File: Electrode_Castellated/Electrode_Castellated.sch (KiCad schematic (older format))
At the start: 21 parts, among them J1 Connector

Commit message: Switch to pogo pin style connector pads
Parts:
- J1: footprint Connector_PinHeader_2.54mm:PinHeader_2x10_P2.54mm_Vertical_SMD -> eaton:Millmax Pad Contacts
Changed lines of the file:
@@
 F 0 "J1" H 3768 4417 50  0000 C CNN
 F 1 "Connector" H 3768 4326 50  0000 C CNN
-F 2 "Connector_PinHeader_2.54mm:PinHeader_2x10_P2.54mm_Vertical_SMD" H 3850 3300 50  0001 C CNN
+F 2 "eaton:Millmax Pad Contacts" H 3850 3300 50  0001 C CNN
 F 3 "~" H 3850 3300 50  0001 C CNN
 	1    3850 3300

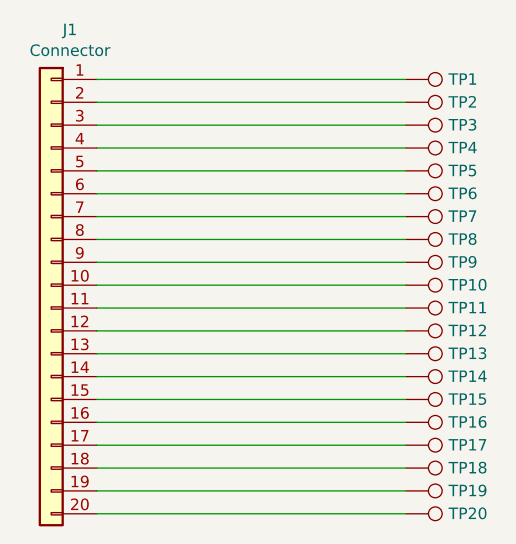
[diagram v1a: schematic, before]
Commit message: Fix silkscreen labels, add dimensions & SN
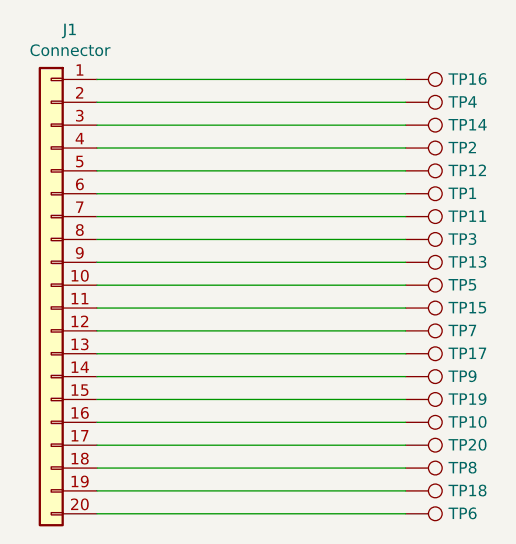
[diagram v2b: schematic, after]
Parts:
- renumbered TP6 to TP1, TP16 to TP10, TP7 to TP11, TP5 to TP12, TP9 to TP13, TP3 to TP14, TP11 to TP15, TP1 to TP16, TP13 to TP17, TP19 to TP18, TP15 to TP19, TP4 to TP2, TP17 to TP20, TP8 to TP3, TP2 to TP4, TP10 to TP5, TP20 to TP6, TP12 to TP7, TP18 to TP8, TP14 to TP9
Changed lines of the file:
@@
 $EndComp
 $Comp
-L Connector:TestPoint TP1
+L Connector:TestPoint TP16
 U 1 1 5F342D33
 P 5400 2400
-F 0 "TP1" V 5400 2588 50  0000 L CNN
+F 0 "TP16" V 5400 2588 50  0000 L CNN
 F 1 "1" V 5445 2588 50  0001 L CNN
 F 2 "TestPoint:TestPoint_THTPad_D2.0mm_Drill1.0mm" H 5600 2400 50  0001 C CNN
@@
 $EndComp
 $Comp
-L Connector:TestPoint TP2
+L Connector:TestPoint TP4
 U 1 1 5F343593
 P 5400 2500
-F 0 "TP2" V 5400 2688 50  0000 L CNN
+F 0 "TP4" V 5400 2688 50  0000 L CNN
 F 1 "2" V 5445 2688 50  0001 L CNN
 F 2 "TestPoint:TestPoint_THTPad_D2.0mm_Drill1.0mm" H 5600 2500 50  0001 C CNN
@@
 $EndComp
 $Comp
-L Connector:TestPoint TP3
+L Connector:TestPoint TP14
 U 1 1 5F343780
 P 5400 2600
-F 0 "TP3" V 5400 2788 50  0000 L CNN
+F 0 "TP14" V 5400 2788 50  0000 L CNN
 F 1 "3" V 5445 2788 50  0001 L CNN
 F 2 "TestPoint:TestPoint_THTPad_D2.0mm_Drill1.0mm" H 5600 2600 50  0001 C CNN
@@
 $EndComp
 $Comp
-L Connector:TestPoint TP4
+L Connector:TestPoint TP2
 U 1 1 5F34388B
 P 5400 2700
-F 0 "TP4" V 5400 2888 50  0000 L CNN
+F 0 "TP2" V 5400 2888 50  0000 L CNN
 F 1 "4" V 5445 2888 50  0001 L CNN
 F 2 "TestPoint:TestPoint_THTPad_D2.0mm_Drill1.0mm" H 5600 2700 50  0001 C CNN
@@
 $EndComp
 $Comp
-L Connector:TestPoint TP5
+L Connector:TestPoint TP12
 U 1 1 5F343A54
 P 5400 2800
-F 0 "TP5" V 5400 2988 50  0000 L CNN
+F 0 "TP12" V 5400 2988 50  0000 L CNN
 F 1 "5" V 5445 2988 50  0001 L CNN
 F 2 "TestPoint:TestPoint_THTPad_D2.0mm_Drill1.0mm" H 5600 2800 50  0001 C CNN
@@
 $EndComp
 $Comp
-L Connector:TestPoint TP6
+L Connector:TestPoint TP1
 U 1 1 5F343BE0
 P 5400 2900
-F 0 "TP6" V 5400 3088 50  0000 L CNN
+F 0 "TP1" V 5400 3088 50  0000 L CNN
 F 1 "6" V 5445 3088 50  0001 L CNN
 F 2 "TestPoint:TestPoint_THTPad_D2.0mm_Drill1.0mm" H 5600 2900 50  0001 C CNN
@@
 $EndComp
 $Comp
-L Connector:TestPoint TP7
+L Connector:TestPoint TP11
 U 1 1 5F343DB4
 P 5400 3000
-F 0 "TP7" V 5400 3188 50  0000 L CNN
+F 0 "TP11" V 5400 3188 50  0000 L CNN
 F 1 "7" V 5445 3188 50  0001 L CNN
 F 2 "TestPoint:TestPoint_THTPad_D2.0mm_Drill1.0mm" H 5600 3000 50  0001 C CNN
@@
 $EndComp
 $Comp
-L Connector:TestPoint TP8
+L Connector:TestPoint TP3
 U 1 1 5F343FB3
 P 5400 3100
-F 0 "TP8" V 5400 3288 50  0000 L CNN
+F 0 "TP3" V 5400 3288 50  0000 L CNN
 F 1 "8" V 5445 3288 50  0001 L CNN
 F 2 "TestPoint:TestPoint_THTPad_D2.0mm_Drill1.0mm" H 5600 3100 50  0001 C CNN
@@
 $EndComp
 $Comp
-L Connector:TestPoint TP9
+L Connector:TestPoint TP13
 U 1 1 5F344129
 P 5400 3200
-F 0 "TP9" V 5400 3388 50  0000 L CNN
+F 0 "TP13" V 5400 3388 50  0000 L CNN
 F 1 "9" V 5445 3388 50  0001 L CNN
 F 2 "TestPoint:TestPoint_THTPad_D2.0mm_Drill1.0mm" H 5600 3200 50  0001 C CNN
@@
 $EndComp
 $Comp
-L Connector:TestPoint TP10
+L Connector:TestPoint TP5
 U 1 1 5F34431B
 P 5400 3300
-F 0 "TP10" V 5400 3488 50  0000 L CNN
+F 0 "TP5" V 5400 3488 50  0000 L CNN
 F 1 "10" V 5445 3488 50  0001 L CNN
 F 2 "TestPoint:TestPoint_THTPad_D2.0mm_Drill1.0mm" H 5600 3300 50  0001 C CNN
@@
 $EndComp
 $Comp
-L Connector:TestPoint TP11
+L Connector:TestPoint TP15
 U 1 1 5F3444FF
 P 5400 3400
-F 0 "TP11" V 5400 3588 50  0000 L CNN
+F 0 "TP15" V 5400 3588 50  0000 L CNN
 F 1 "11" V 5445 3588 50  0001 L CNN
 F 2 "TestPoint:TestPoint_THTPad_D2.0mm_Drill1.0mm" H 5600 3400 50  0001 C CNN
@@
 $EndComp
 $Comp
-L Connector:TestPoint TP12
+L Connector:TestPoint TP7
 U 1 1 5F3446E4
 P 5400 3500
-F 0 "TP12" V 5400 3688 50  0000 L CNN
+F 0 "TP7" V 5400 3688 50  0000 L CNN
 F 1 "12" V 5445 3688 50  0001 L CNN
 F 2 "TestPoint:TestPoint_THTPad_D2.0mm_Drill1.0mm" H 5600 3500 50  0001 C CNN
@@
 $EndComp
 $Comp
-L Connector:TestPoint TP13
+L Connector:TestPoint TP17
 U 1 1 5F344915
 P 5400 3600
-F 0 "TP13" V 5400 3788 50  0000 L CNN
+F 0 "TP17" V 5400 3788 50  0000 L CNN
 F 1 "13" V 5445 3788 50  0001 L CNN
 F 2 "TestPoint:TestPoint_THTPad_D2.0mm_Drill1.0mm" H 5600 3600 50  0001 C CNN
@@
 $EndComp
 $Comp
-L Connector:TestPoint TP14
+L Connector:TestPoint TP9
 U 1 1 5F344AF1
 P 5400 3700
-F 0 "TP14" V 5400 3888 50  0000 L CNN
+F 0 "TP9" V 5400 3888 50  0000 L CNN
 F 1 "14" V 5445 3888 50  0001 L CNN
 F 2 "TestPoint:TestPoint_THTPad_D2.0mm_Drill1.0mm" H 5600 3700 50  0001 C CNN
@@
 $EndComp
 $Comp
-L Connector:TestPoint TP16
+L Connector:TestPoint TP10
 U 1 1 5F344D0B
 P 5400 3900
-F 0 "TP16" V 5400 4088 50  0000 L CNN
+F 0 "TP10" V 5400 4088 50  0000 L CNN
 F 1 "16" V 5445 4088 50  0001 L CNN
 F 2 "TestPoint:TestPoint_THTPad_D2.0mm_Drill1.0mm" H 5600 3900 50  0001 C CNN
@@
 $EndComp
 $Comp
-L Connector:TestPoint TP15
+L Connector:TestPoint TP19
 U 1 1 5F344F73
 P 5400 3800
-F 0 "TP15" V 5400 3988 50  0000 L CNN
+F 0 "TP19" V 5400 3988 50  0000 L CNN
 F 1 "15" V 5445 3988 50  0001 L CNN
 F 2 "TestPoint:TestPoint_THTPad_D2.0mm_Drill1.0mm" H 5600 3800 50  0001 C CNN
@@
 $EndComp
 $Comp
-L Connector:TestPoint TP17
+L Connector:TestPoint TP20
 U 1 1 5F345DC5
 P 5400 4000
-F 0 "TP17" V 5400 4188 50  0000 L CNN
+F 0 "TP20" V 5400 4188 50  0000 L CNN
 F 1 "17" V 5445 4188 50  0001 L CNN
 F 2 "TestPoint:TestPoint_THTPad_D2.0mm_Drill1.0mm" H 5600 4000 50  0001 C CNN
@@
 $EndComp
 $Comp
-L Connector:TestPoint TP18
+L Connector:TestPoint TP8
 U 1 1 5F346015
 P 5400 4100
-F 0 "TP18" V 5400 4288 50  0000 L CNN
+F 0 "TP8" V 5400 4288 50  0000 L CNN
 F 1 "18" V 5445 4288 50  0001 L CNN
 F 2 "TestPoint:TestPoint_THTPad_D2.0mm_Drill1.0mm" H 5600 4100 50  0001 C CNN
@@
 $EndComp
 $Comp
-L Connector:TestPoint TP19
+L Connector:TestPoint TP18
 U 1 1 5F3462CF
 P 5400 4200
-F 0 "TP19" V 5400 4388 50  0000 L CNN
+F 0 "TP18" V 5400 4388 50  0000 L CNN
 F 1 "19" V 5445 4388 50  0001 L CNN
 F 2 "TestPoint:TestPoint_THTPad_D2.0mm_Drill1.0mm" H 5600 4200 50  0001 C CNN
@@
 $EndComp
 $Comp
-L Connector:TestPoint TP20
+L Connector:TestPoint TP6
 U 1 1 5F346555
 P 5400 4300
-F 0 "TP20" V 5400 4488 50  0000 L CNN
+F 0 "TP6" V 5400 4488 50  0000 L CNN
 F 1 "30" V 5445 4488 50  0001 L CNN
 F 2 "TestPoint:TestPoint_THTPad_D2.0mm_Drill1.0mm" H 5600 4300 50  0001 C CNN
